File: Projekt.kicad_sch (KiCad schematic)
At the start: 60 parts, among them Q1 CSD19505, Q4 Si2306, Q5 2N3904, Q6 2N3904, U1 ACS712, U10 ADS1015, U2 B1212S, U3 AMS1117-5.0, U4 AMS1117-3.3, U5 XL7005A, U6 XL7005A, U7 IR2104, U9 CH340G

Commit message: Schaltplan fertig ?
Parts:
- added C12, C13, C23: 100nF, symbol Device:C_Small
- added C19: 470nF, symbol Device:C_Small
- added C8: 470uF, symbol Device:C_Polarized
- added D1, D2: SS310, Diode_SMD:D_SMB, symbol footprint:SS310
- added D?: 1N4007, Diode_THT:D_DO-41_SOD81_P10.16mm_Horizontal, symbol Diode:1N4007
- added F?: Fuse, symbol Device:Fuse
- added J?: INTERFACE PORT, symbol Connector:Conn_01x08_Male
- added J?: Battery, symbol Connector:Screw_Terminal_01x02
- added L1: 60uH, Inductor_THT:L_Toroid_Vertical_L21.6mm_W11.4mm_P7.62mm_Pulse_KM-3, symbol footprint:SMD_INDUCTOR_CD54
- added LED1: LED, symbol Device:LED
- added Q2, Q3: CSD19505, Package_TO_SOT_THT:TO-220-3_Vertical, symbol Transistor_FET:CSD19502Q5B
- added R10, R9: 100, symbol Device:R_Small
- added R11, R8: 100k, symbol Device:R_Small
- added R12, R21, R24, R29, R30, R36: 10k, symbol Device:R_Small
- added R32, R33: 47k, symbol Device:R_Small
- added R34: 1k, symbol Device:R_Small
- added R35: 10k, symbol Device:Thermistor_NTC
- added U8: ESP32, RF_Module:ESP32-WROOM-32, symbol RF_Module:ESP32-WROOM-32
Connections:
- net +3.3V: now also C23.2, J?.2 (Pin_2), R21.1, R24.2, R35.2, U8.2 (VDD)
- net A1: now also C13.1, R32.2, R33.2, R34.1
- net GND: now also J?.1 (Pin_1), C12.2, C13.2, C19.1, C23.1, C8.2, D?.1 (K), J?.1 (Pin_1), J?.1 (Pin_1), Q3.1 (S), Q3.2 (S), Q3.3 (S), R11.2, R12.2, R29.1, R30.1, R34.2, R36.1, U8.1 (GND), U8.15 (GND), U8.38 (GND), U8.39 (GND); no longer J?.2 (Pin_2)
- net GPIO27: now also U8.12 (IO27)
- net GPIO32: now also U8.8 (IO32)
- net GPIO33: now also U8.9 (IO33)
- net GPIO34: now also U8.6 (IO34)
- net SCL: now also J?.4 (Pin_4), R29.2, U8.36 (IO22)
- net SDA: now also J?.3 (Pin_3), R30.2, U8.33 (IO21)
- net at U7.5 (LO): now also D2.A1 (Anode), R10.1
- net at C10.2, U7.6 (VS): now also L1.1, Q2.1 (S), Q2.2 (S), Q2.3 (S), Q3.5 (D), R8.2
- net at U7.7 (HO): now also D1.A1 (Anode), R9.1
- net at Q1.5 (D): now also Q2.5 (D)
- net at D8.2 (A), F?.1: now also J?.2 (Pin_2); no longer J?.1 (Pin_1)
- net ESP EN renamed EN
- net EN: now also C19.2, R21.2, U8.3 (EN)
- net ESP GPIO0 renamed GPIO0
- net GPIO0: now also R24.1, U8.25 (IO0)
- net ESP RX renamed RX
- net RX: now also U8.34 (RXD0/IO3)
- net ESP TX renamed TX
- net TX: now also U8.35 (TXD0/IO1)
- new net: C8.1, F?.2, L1.2, R32.1, R33.1
- new net: D2.A2 (Katode), Q3.4 (G), R10.2, R11.1
- new net: C12.1, R12.1, R35.1, U8.7 (IO35)
- new net: D1.A2 (Katode), Q2.4 (G), R8.1, R9.2
- new net: D?.2 (A), F?.1, J?.2 (Pin_2)
- new net: LED1.1 (K), R36.2
- new net: LED1.2 (A), U8.24 (IO2)
- new net GPIO17: J?.5 (Pin_5), U8.28 (IO17)
- new net GPIO18: J?.6 (Pin_6), U8.30 (IO18)
- new net GPIO19: J?.7 (Pin_7), U8.31 (IO19)
- new net GPIO23: J?.8 (Pin_8), U8.37 (IO23)
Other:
- moved on the sheet: C3, C4, J?, LED2, Q4, R6, R7, U2

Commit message: Layouten...
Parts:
- removed Q1, Q2, Q3: CSD19505, Package_TO_SOT_THT:TO-220-3_Vertical, symbol Transistor_FET:CSD19502Q5B
- removed Q4: Si2306, Package_TO_SOT_SMD:SOT-23, symbol Transistor_FET:CSD19502Q5B
- added J5: FAN, Connector_PinHeader_2.54mm:PinHeader_1x02_P2.54mm_Vertical, symbol Connector:Conn_01x02_Male
- added Q1, Q2, Q3: CSD19505KCS, Package_TO_SOT_THT:TO-220-3_Vertical, symbol footprint:CSD19505KCS
- added Q4, Q7: Si2306, Package_TO_SOT_SMD:SOT-23, symbol footprint:CSD19505KCS
- added R25: 10k, Resistor_SMD:R_0805_2012Metric, symbol Device:R_Small
- C1, C12, C13, C15, C17, C19, C2, C20, C23, C3, C4: footprint (none) -> Capacitor_SMD:C_0603_1608Metric
- C10: footprint (none) -> Capacitor_SMD:C_Elec_5x5.4
- C14: footprint (none) -> Capacitor_SMD:C_Elec_6.3x5.8; Voltage (none) -> 16V
- C16: footprint (none) -> Capacitor_SMD:C_Elec_6.3x5.8
- C18: footprint (none) -> Capacitor_SMD:C_Elec_6.3x5.8; Voltage (none) -> 80V
- C21, C22, C5, C6: footprint (none) -> Capacitor_SMD:C_0805_2012Metric
- C7: footprint (none) -> Capacitor_THT:C_Radial_D12.5mm_H20.0mm_P5.00mm; Voltage (none) -> 80V
- C8: footprint (none) -> Capacitor_THT:C_Radial_D12.5mm_H20.0mm_P5.00mm
- C9: renamed from C2; footprint (none) -> Capacitor_SMD:C_0805_2012Metric
- D4: renamed from D?; footprint Diode_THT:D_DO-41_SOD81_P10.16mm_Horizontal -> Diode_SMD:D_SMC
- D8: footprint Diode_THT:D_DO-41_SOD81_P10.16mm_Horizontal -> Diode_SMD:D_SMC
- F1, F2: renamed from F?; footprint (none) -> Fuse:Fuse_Blade_ATO_directSolder
- J1, J2: renamed from J?; footprint (none) -> TerminalBlock_WAGO:TerminalBlock_WAGO_236-602_1x02_P10.00mm_45Degree
- J3: renamed from J?; footprint (none) -> Connector_USB:USB_Mini-B_Lumberg_2486_01_Horizontal
- J4: renamed from J?; footprint (none) -> Connector_PinHeader_2.54mm:PinHeader_1x08_P2.54mm_Vertical
- LED1, LED2: footprint (none) -> LED_SMD:LED_0805_2012Metric
- Q5, Q6: value 2N3904 -> MMBT3904 1A; footprint Package_TO_SOT_THT:TO-92_Inline -> Package_TO_SOT_SMD:SOT-23
- R1, R10, R11, R12, R13, R14, R15, R16, R17, R18, R19, R2, R20, R21, R22, R23, R24, R29, R3, R30, R31, R32, R33, R34, R35, R36, R37, R4, R5, R6, R7, R8, R9: footprint (none) -> Resistor_SMD:R_0805_2012Metric
- U2: footprint 1x04_P2.50mm -> Connector_PinHeader_2.54mm:PinHeader_1x04_P2.54mm_Vertical
- U7: footprint (none) -> Package_SO:SOIC-8_3.9x4.9mm_P1.27mm
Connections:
- net +12V: now also D3.1 (Katode), U2.2 (VIN), J5.1 (Pin_1); no longer D3.A2 (Katode)
- net +3.3V: now also D7.2 (Anode); no longer D7.A1 (Anode)
- net GND: now also D5.1 (Katode), D6.1 (Katode), Q3.3 (S), Q4.3 (S), Q7.3 (S), R25.2; no longer C1.2, D4.1 (K), D5.A2 (Katode), D6.A2 (Katode), D8.1 (K)
- net GPIO27: now also Q4.1 (G)
- net at C18.1, U5.1 (VIN), U6.1 (VIN): now also D4.1 (K), D8.1 (K)
- net at L2.1, U5.2 (SW): now also D5.2 (Anode); no longer D5.A1 (Anode)
- net at R10.1, U7.5 (LO): now also D2.2 (Anode); no longer D2.A1 (Anode)
- net at R10.2, R11.1: now also D2.1 (Katode), Q3.1 (G); no longer D2.A2 (Katode)
- net at C22.1, U4.2 (VO): now also D7.1 (Katode); no longer D7.A2 (Katode)
- net at C4.1, R37.2, R6.2: now also U2.4 (VOUT), Q1.1 (G)
- net at C4.2, LED2.1 (K), R37.1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: now also U2.3 (GND2), Q1.3 (S)
- net at C10.2, L1.1, R8.2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: now also Q2.3 (S), Q3.2 (D)
- net at R9.1, U7.7 (HO): now also D1.2 (Anode); no longer D1.A1 (Anode)
- net at C10.1, U7.8 (VB): now also D3.2 (Anode); no longer D3.A1 (Anode)
- net at C3.2: now also U2.1 (GND), Q4.2 (D)
- net at R8.1, R9.2: now also D1.1 (Katode), Q2.1 (G); no longer D1.A2 (Katode)
- net at L3.1, U6.2 (SW): now also D6.2 (Anode); no longer D6.A1 (Anode)
- net at U8.27 (IO16): now also Q7.1 (G), R25.1
- net A0: no longer names the net of U10.4 (AIN0)
- new net: J5.2 (Pin_2), Q7.2 (D)
- new net: Q1.2 (D), Q2.2 (D)
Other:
- note added: "2N3904"
- note added: "BACKFLOW CURRENT CONTROL UNIT (BCCU)"
- note added: "INPUT CURRENT SENSOR"
- note added: "INPUT VOLTAGE DIVIDER"
- note added: "MOS DRIVER (BUCK DRIVER)"
- moved on the sheet: C1, C10, C12, C13, C14, C15, C16, C17, C19, C2, C20, C21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

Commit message: So gut wie fertig ... ?
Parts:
- added J6: JTAG, Connector_PinHeader_1.27mm:PinHeader_2x05_P1.27mm_Vertical_SMD, symbol Connector_Generic:Conn_02x05_Odd_Even
- D4, D8: footprint Diode_SMD:D_SMC -> Diode_SMD:D_SMB
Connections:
- net +3.3V: now also J6.1 (Pin_1); no longer J4.2 (Pin_2)
- net +5V: now also J4.2 (Pin_2)
- net GND: now also J6.3 (Pin_3), J6.5 (Pin_5), J6.9 (Pin_9)
- net at U8.13 (IO14): now also J6.2 (Pin_2)
- net at U8.14 (IO12): now also J6.8 (Pin_8)
- net at U8.16 (IO13): now also J6.4 (Pin_4)
- net at U8.23 (IO15): now also J6.6 (Pin_6)
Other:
- moved on the sheet: J5, LED1, Q7, R25, R36

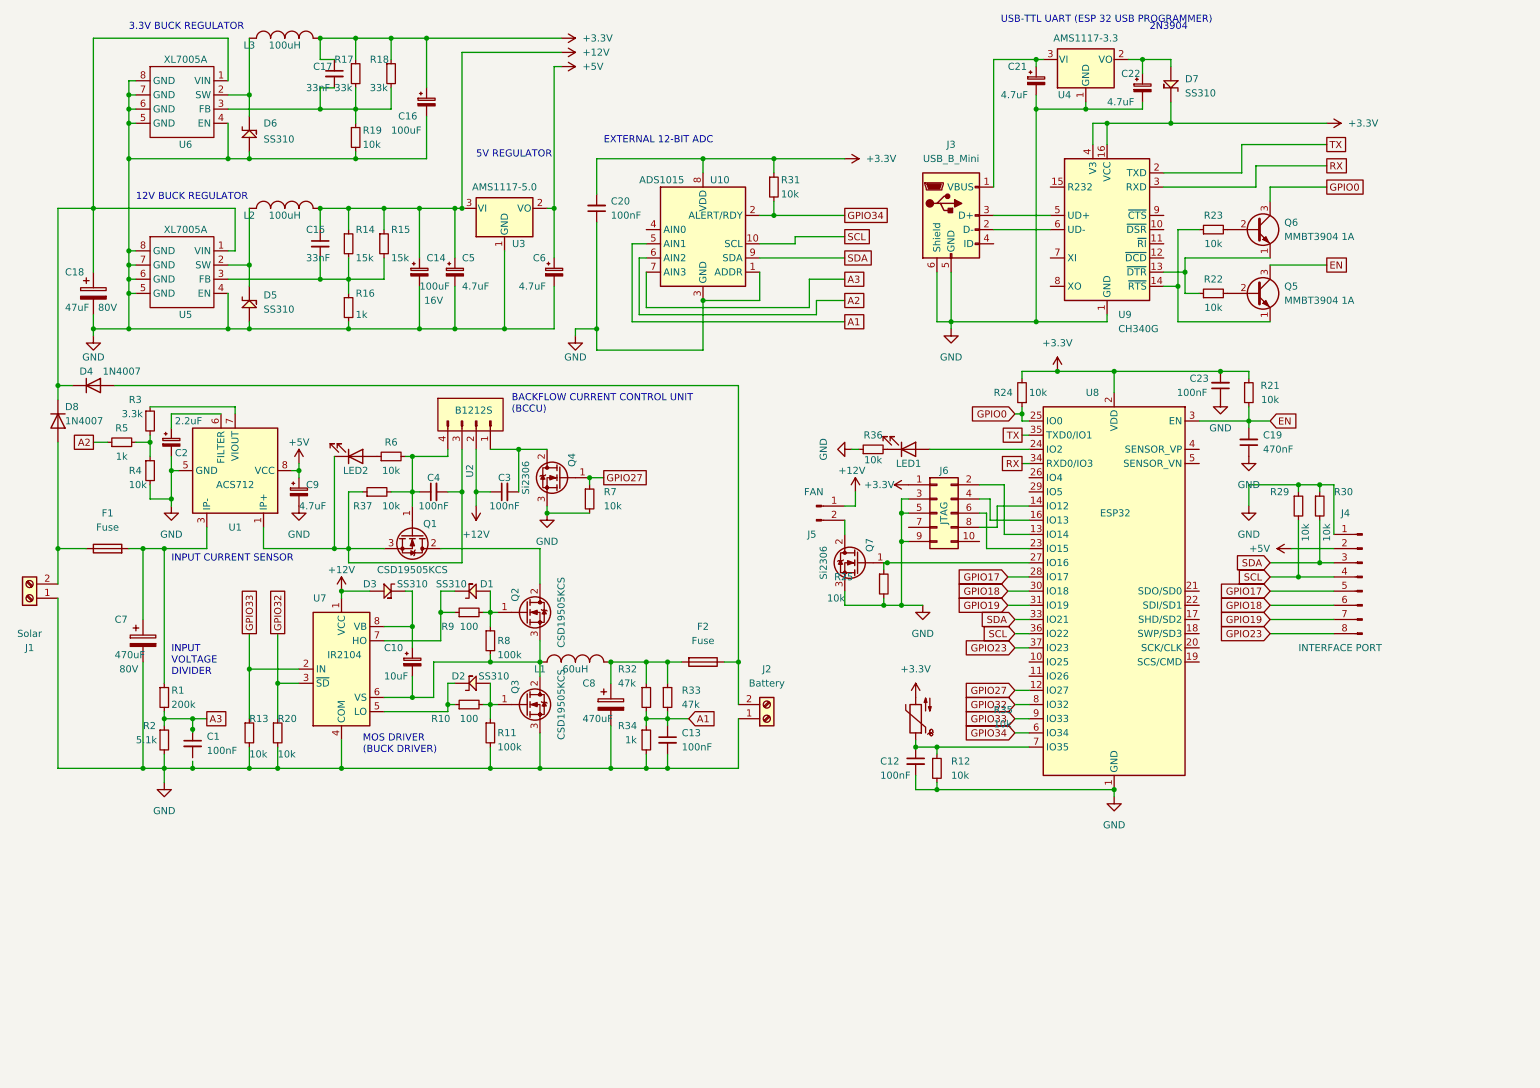
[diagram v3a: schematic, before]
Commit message: Leiterbahnen verstärkt
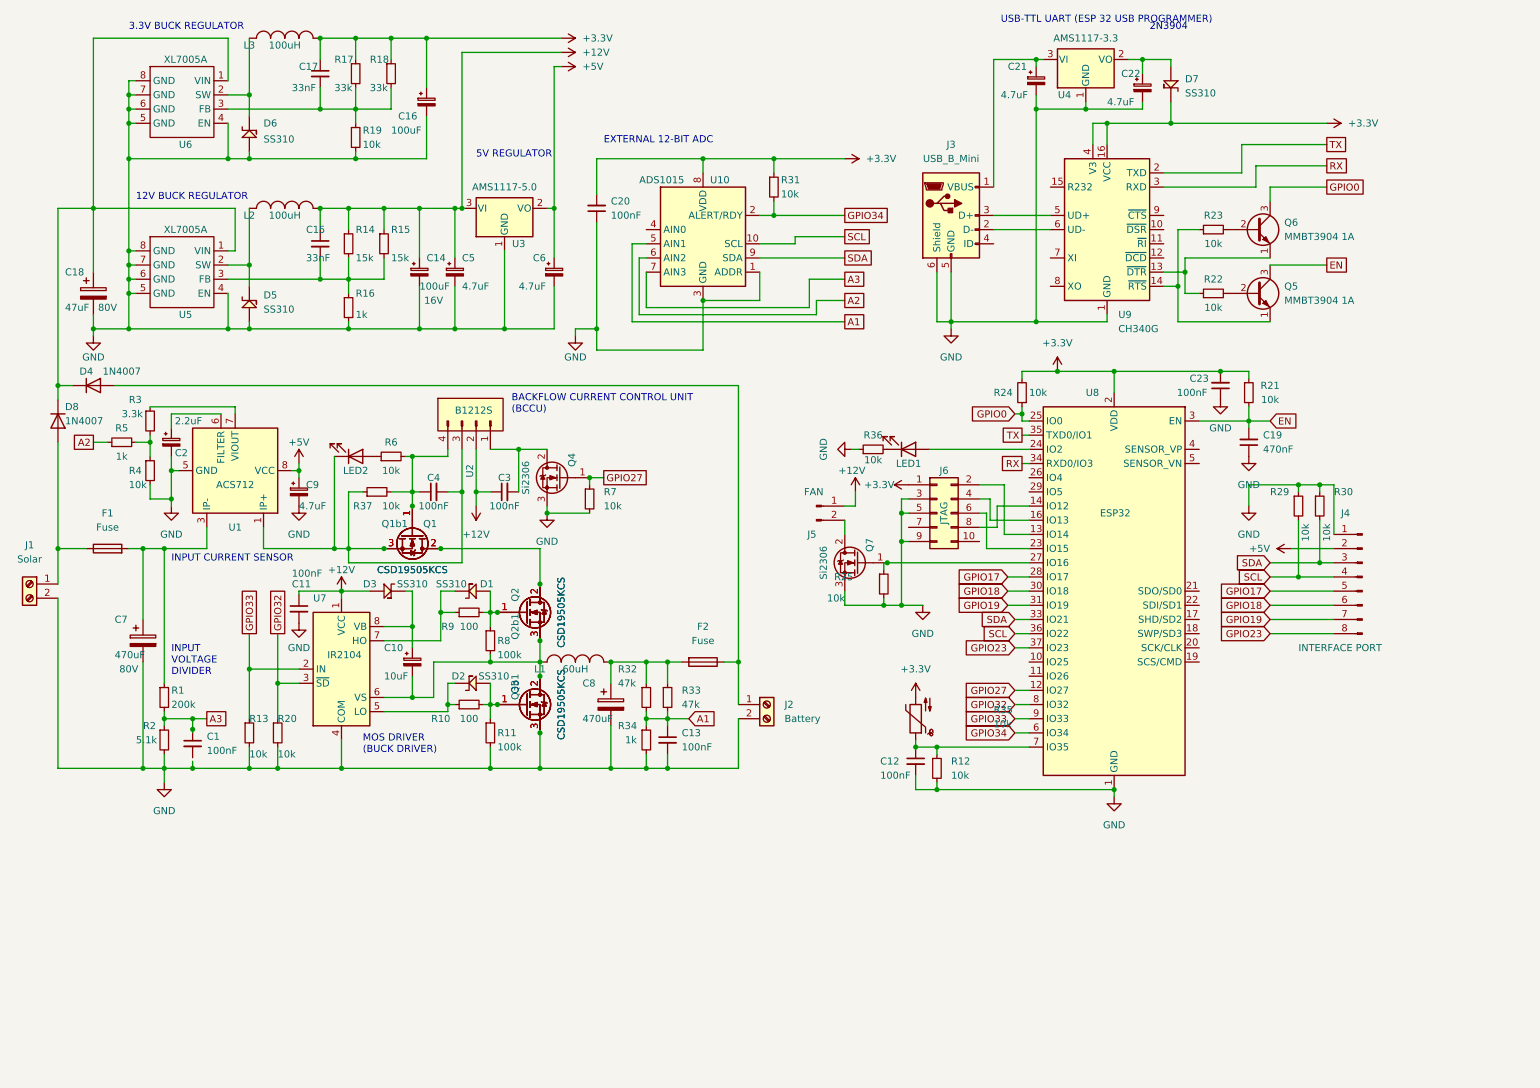
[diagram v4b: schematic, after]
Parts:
- added C11: 100nF, Capacitor_SMD:C_0603_1608Metric, symbol Device:C_Small
- added Q1b1, Q2b1, Q3b1: CSD19505KCS, Package_TO_SOT_THT:TO-220-3_Vertical, symbol footprint:CSD19505KCS
- J1, J2: footprint TerminalBlock_WAGO:TerminalBlock_WAGO_236-602_1x02_P10.00mm_45Degree -> footprints:TerminalBlock_DEGSON_DG135T
- R35: footprint Resistor_SMD:R_0805_2012Metric -> Connector_PinHeader_2.54mm:PinHeader_1x02_P2.54mm_Vertical
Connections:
- net +12V: now also C11.1
- net GND: now also J1.2 (Pin_2), J2.2 (Pin_2), C11.2, Q3b1.3 (S); no longer J1.1 (Pin_1), J2.1 (Pin_1)
- net at D2.1 (Katode), Q3.1 (G), R10.2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: now also Q3b1.1 (G)
- net at C4.1, Q1.1 (G), R37.2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: now also Q1b1.1 (G)
- net at C4.2, LED2.1 (K), Q1.3 (S)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: now also Q1b1.3 (S)
- net at C10.2, L1.1, Q2.3 (S)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: now also Q2b1.3 (S), Q3b1.2 (D)
- net at D1.1 (Katode), Q2.1 (G), R8.1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: now also Q2b1.1 (G)
- net at D4.2 (A), F2.1: now also J2.1 (Pin_1); no longer J2.2 (Pin_2)
- net at Q1.2 (D), Q2.2 (D): now also Q1b1.2 (D), Q2b1.2 (D)
- net at D8.2 (A), F1.1: now also J1.1 (Pin_1); no longer J1.2 (Pin_2)
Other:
- moved on the sheet: C17, J1
